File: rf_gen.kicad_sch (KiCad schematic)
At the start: 43 parts, among them J1 Conn_01x07_Male, J2 Conn_01x02_Female, J3 Conn_01x05_Male, J4 Jack-DC, Q1 GS61004B, Q2 G3R350MT12J, U1 NPC81074, U2 AP62150

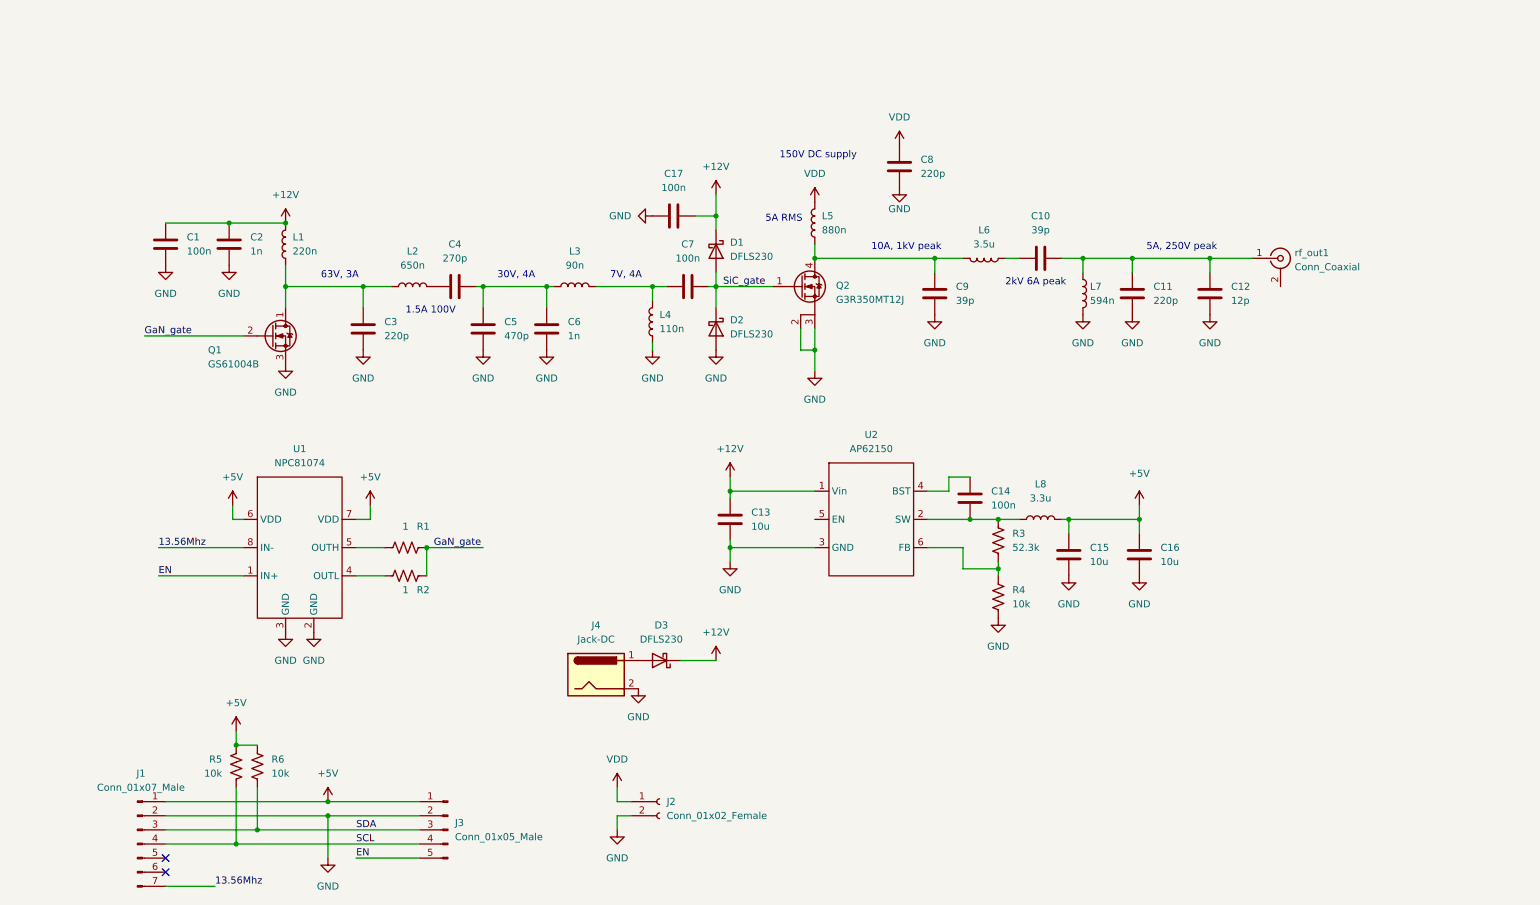
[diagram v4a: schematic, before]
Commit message: Added netclasses, test points, fixed buck regulator
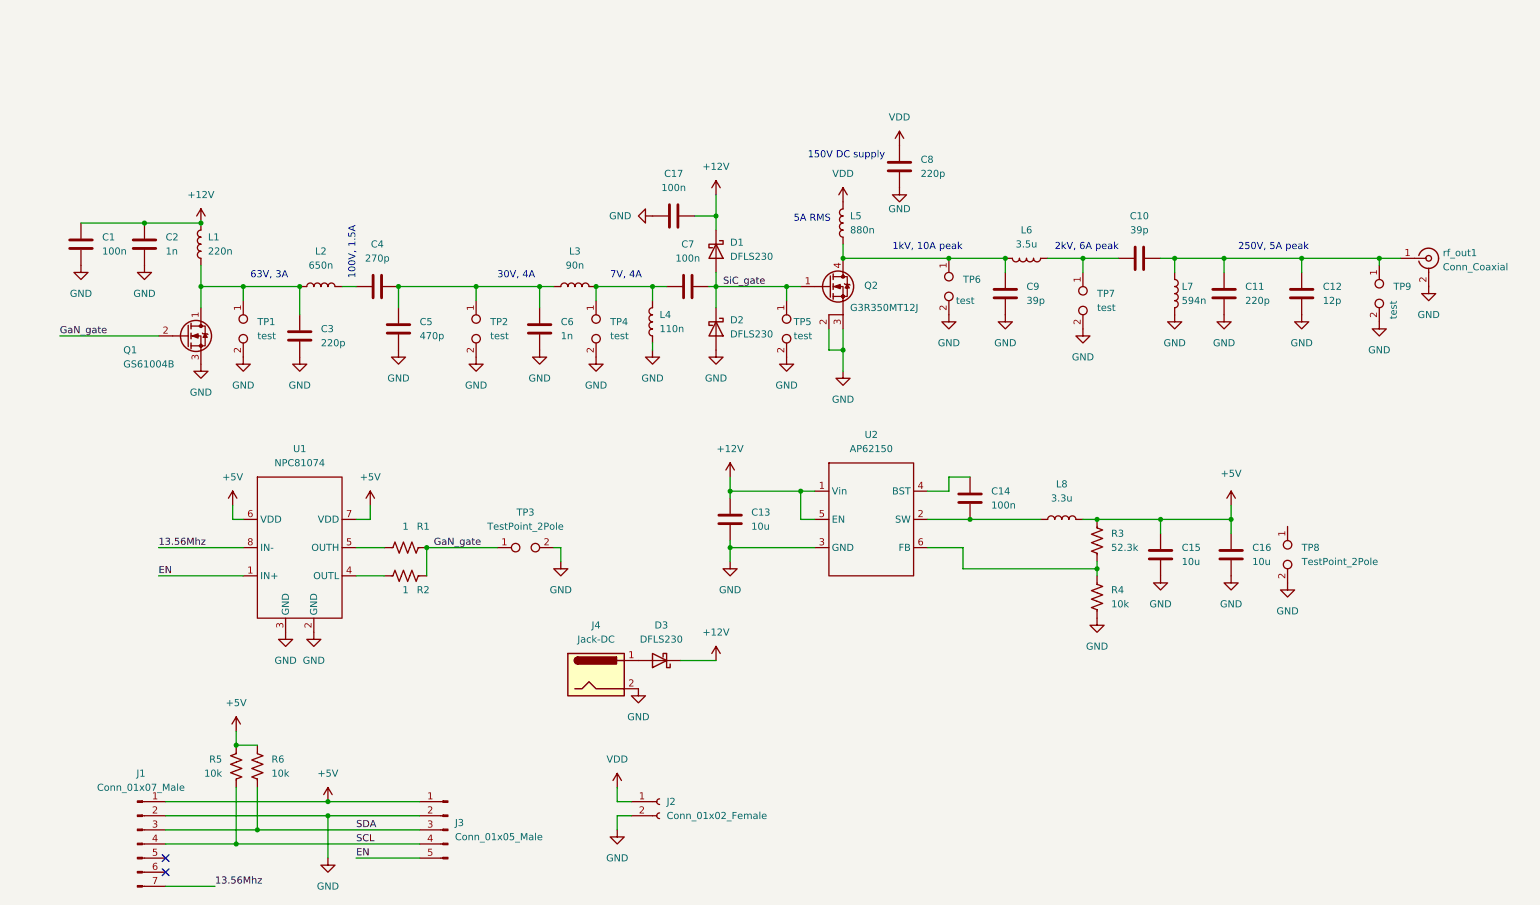
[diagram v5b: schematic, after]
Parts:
- added TP1, TP2, TP4, TP5, TP6, TP7, TP9: test, symbol Connector:TestPoint_2Pole
- added TP3, TP8: TestPoint_2Pole, symbol Connector:TestPoint_2Pole
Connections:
- net +12V: now also U2.5 (EN)
- net +5V: now also R3.1
- net GND: now also rf_out1.2 (Ext), TP1.2, TP2.2, TP3.2, TP4.2, TP5.2, TP6.2, TP7.2, TP8.2, TP9.2
- net GaN_gate: now also TP3.1
- net SiC_gate: now also TP5.1
- net at C4.2, C5.1, C6.1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: now also TP2.1
- net at C7.2, L3.2, L4.2: now also TP4.1
- net at C14.2, L8.1, U2.2 (SW): no longer R3.1
- net at C10.2, C11.1, C12.1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: now also TP9.1
- net at C3.2, L1.1, L2.1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: now also TP1.1
- net at C9.2, L5.1, L6.2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: now also TP6.1
- net at C10.1, L6.1: now also TP7.1
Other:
- note added: "100V, 1.5A"
- note added: "1kV, 10A peak"
- note added: "250V, 5A peak"
- note added: "2kV, 6A peak"
- note removed: "1.5A 100V"
- note removed: "10A, 1kV peak"
- note removed: "2kV 6A peak"
- note removed: "5A, 250V peak"
- moved on the sheet: C1, C10, C11, C12, C15, C16, C2, C3, C4, C5, C6, C9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

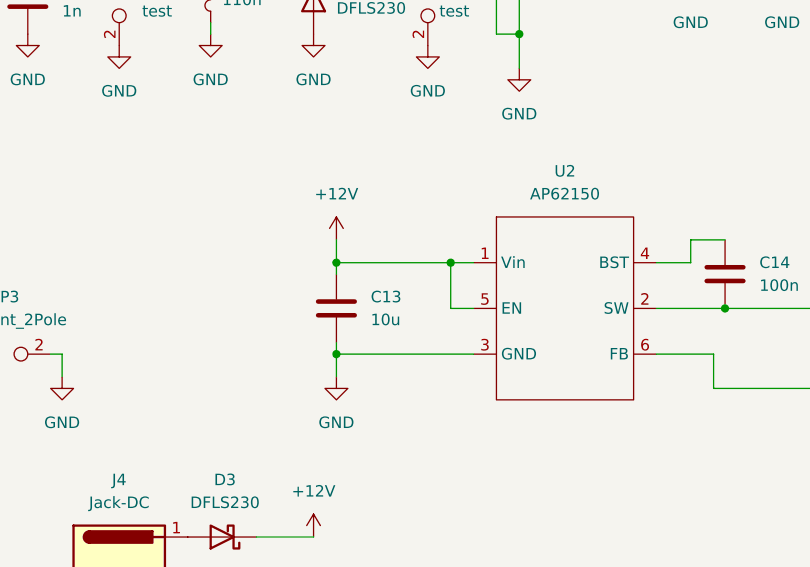
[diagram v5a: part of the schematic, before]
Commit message: Draft of trace routing
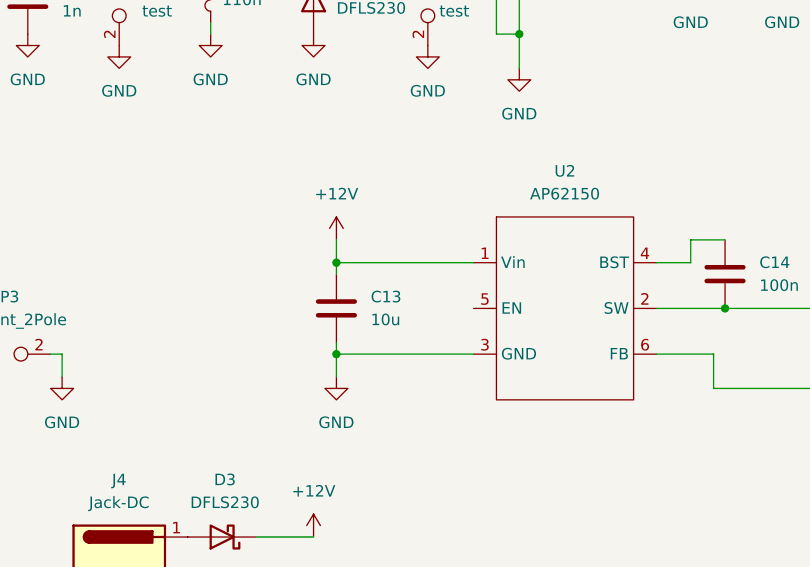
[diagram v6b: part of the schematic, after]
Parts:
- TP1, TP2, TP3, TP4, TP5, TP6, TP7, TP8, TP9: footprint (none) -> TestPoint:TestPoint_2Pads_Pitch5.08mm_Drill1.3mm
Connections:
- net +12V: no longer U2.5 (EN)
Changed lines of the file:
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@@
 (kicad_sch (version 20211123) (generator eeschema)
   (paper "A4")
-  (junction (at 157.48 116.84) (diameter 0) (color 0 0 0 0)
-  )
   (junction (at 110.49 80.01) (diameter 0) (color 0 0 0 0)
   )
@@
     (stroke (width 0) (type default) (color 0 0 0 0))
   )
-  (wire (pts (xy 157.48 121.92) (xy 157.48 116.84))
-    (stroke (width 0) (type default) (color 0 0 0 0))
-  )
   (wire (pts (xy 55.88 162.56) (xy 59.69 162.56))
     (stroke (width 0) (type default) (color 0 0 0 0))
@@
     (stroke (width 0) (type default) (color 0 0 0 0))
   )
-  (wire (pts (xy 144.78 116.84) (xy 157.48 116.84))
-    (stroke (width 0) (type default) (color 0 0 0 0))
-  )
   (wire (pts (xy 201.93 74.93) (xy 208.28 74.93))
     (stroke (width 0) (type default) (color 0 0 0 0))
@@
     (stroke (width 0) (type default) (color 0 0 0 0))
   )
-  (wire (pts (xy 160.02 121.92) (xy 157.48 121.92))
-    (stroke (width 0) (type default) (color 0 0 0 0))
-  )
   (wire (pts (xy 77.47 80.01) (xy 74.93 80.01))
     (stroke (width 0) (type default) (color 0 0 0 0))
@@
     (stroke (width 0) (type default) (color 0 0 0 0))
   )
-  (wire (pts (xy 157.48 116.84) (xy 160.02 116.84))
+  (wire (pts (xy 144.78 116.84) (xy 160.02 116.84))
     (stroke (width 0) (type default) (color 0 0 0 0))
   )
@@
       (effects (font (size 1.27 1.27)) (justify left))
     )
-    (property "Footprint" "" (id 2) (at 245.11 128.27 0)
+    (property "Footprint" "TestPoint:TestPoint_2Pads_Pitch5.08mm_Drill1.3mm" (id 2) (at 245.11 128.27 0)
       (effects (font (size 1.27 1.27)) hide)
     )
@@
       (effects (font (size 1.27 1.27)) (justify left))
     )
-    (property "Footprint" "" (id 2) (at 99.06 87.63 0)
+    (property "Footprint" "TestPoint:TestPoint_2Pads_Pitch5.08mm_Drill1.3mm" (id 2) (at 99.06 87.63 0)
       (effects (font (size 1.27 1.27)) hide)
     )
@@
       (effects (font (size 1.27 1.27)) (justify left))
     )
-    (property "Footprint" "" (id 2) (at 208.28 82.55 0)
+    (property "Footprint" "TestPoint:TestPoint_2Pads_Pitch5.08mm_Drill1.3mm" (id 2) (at 208.28 82.55 0)
       (effects (font (size 1.27 1.27)) hide)
     )
@@
       (effects (font (size 1.27 1.27)) (justify left))
     )
-    (property "Footprint" "" (id 2) (at 261.62 81.28 0)
+    (property "Footprint" "TestPoint:TestPoint_2Pads_Pitch5.08mm_Drill1.3mm" (id 2) (at 261.62 81.28 0)
       (effects (font (size 1.27 1.27)) hide)
     )
@@
     (property "Reference" "TP3" (id 0) (at 107.95 120.65 0))
     (property "Value" "TestPoint_2Pole" (id 1) (at 107.95 123.19 0))
-    (property "Footprint" "" (id 2) (at 107.95 127 0)
+    (property "Footprint" "TestPoint:TestPoint_2Pads_Pitch5.08mm_Drill1.3mm" (id 2) (at 107.95 127 0)
       (effects (font (size 1.27 1.27)) hide)
     )
@@
       (effects (font (size 1.27 1.27)) (justify left))
     )
-    (property "Footprint" "" (id 2) (at 120.65 87.63 0)
+    (property "Footprint" "TestPoint:TestPoint_2Pads_Pitch5.08mm_Drill1.3mm" (id 2) (at 120.65 87.63 0)
       (effects (font (size 1.27 1.27)) hide)
     )
@@
       (effects (font (size 1.27 1.27)) (justify left))
     )
-    (property "Footprint" "" (id 2) (at 57.15 87.63 0)
+    (property "Footprint" "TestPoint:TestPoint_2Pads_Pitch5.08mm_Drill1.3mm" (id 2) (at 57.15 87.63 0)
       (effects (font (size 1.27 1.27)) hide)
     )
@@
       (effects (font (size 1.27 1.27)) (justify left))
     )
-    (property "Footprint" "" (id 2) (at 184.15 80.01 0)
+    (property "Footprint" "TestPoint:TestPoint_2Pads_Pitch5.08mm_Drill1.3mm" (id 2) (at 184.15 80.01 0)
       (effects (font (size 1.27 1.27)) hide)
     )
@@
       (effects (font (size 1.27 1.27)) (justify left))
     )
-    (property "Footprint" "" (id 2) (at 154.94 87.63 0)
+    (property "Footprint" "TestPoint:TestPoint_2Pads_Pitch5.08mm_Drill1.3mm" (id 2) (at 154.94 87.63 0)
       (effects (font (size 1.27 1.27)) hide)
     )
@@
     )
     (path "/9e46c7f8-a513-4ff2-a7e6-e7adc86b0c60"
-      (reference "TP1") (unit 1) (value "test") (footprint "")
+      (reference "TP1") (unit 1) (value "test") (footprint "TestPoint:TestPoint_2Pads_Pitch5.08mm_Drill1.3mm")
     )
     (path "/380384f8-f2f9-4acb-82c0-d194cb47f844"
-      (reference "TP2") (unit 1) (value "test") (footprint "")
+      (reference "TP2") (unit 1) (value "test") (footprint "TestPoint:TestPoint_2Pads_Pitch5.08mm_Drill1.3mm")
     )
     (path "/75c06a4c-dfd4-4ed7-b3c2-af1e7ac28588"
-      (reference "TP3") (unit 1) (value "TestPoint_2Pole") (footprint "")
+      (reference "TP3") (unit 1) (value "TestPoint_2Pole") (footprint "TestPoint:TestPoint_2Pads_Pitch5.08mm_Drill1.3mm")
     )
     (path "/9a243108-930d-4114-9dcc-3f8fefa4acfd"
-      (reference "TP4") (unit 1) (value "test") (footprint "")
+      (reference "TP4") (unit 1) (value "test") (footprint "TestPoint:TestPoint_2Pads_Pitch5.08mm_Drill1.3mm")
     )
     (path "/e1db0c58-29d8-489b-9a95-02e5bb88fba5"
-      (reference "TP5") (unit 1) (value "test") (footprint "")
+      (reference "TP5") (unit 1) (value "test") (footprint "TestPoint:TestPoint_2Pads_Pitch5.08mm_Drill1.3mm")
     )
     (path "/cb32965e-963f-4082-9e02-ff21cd91984e"
-      (reference "TP6") (unit 1) (value "test") (footprint "")
+      (reference "TP6") (unit 1) (value "test") (footprint "TestPoint:TestPoint_2Pads_Pitch5.08mm_Drill1.3mm")
     )
     (path "/49587f3e-e4fc-4bf0-8d1d-a51cab304d0c"
-      (reference "TP7") (unit 1) (value "test") (footprint "")
+      (reference "TP7") (unit 1) (value "test") (footprint "TestPoint:TestPoint_2Pads_Pitch5.08mm_Drill1.3mm")
     )
     (path "/07035750-a09f-4f0d-b8da-574cc7129fe3"
-      (reference "TP8") (unit 1) (value "TestPoint_2Pole") (footprint "")
+      (reference "TP8") (unit 1) (value "TestPoint_2Pole") (footprint "TestPoint:TestPoint_2Pads_Pitch5.08mm_Drill1.3mm")
     )
     (path "/60d8926b-287a-43ee-89b3-bae467c7fd5e"
-      (reference "TP9") (unit 1) (value "test") (footprint "")
+      (reference "TP9") (unit 1) (value "test") (footprint "TestPoint:TestPoint_2Pads_Pitch5.08mm_Drill1.3mm")
     )
     (path "/05524bb0-81b6-47ef-ac3c-1b815742ae84"

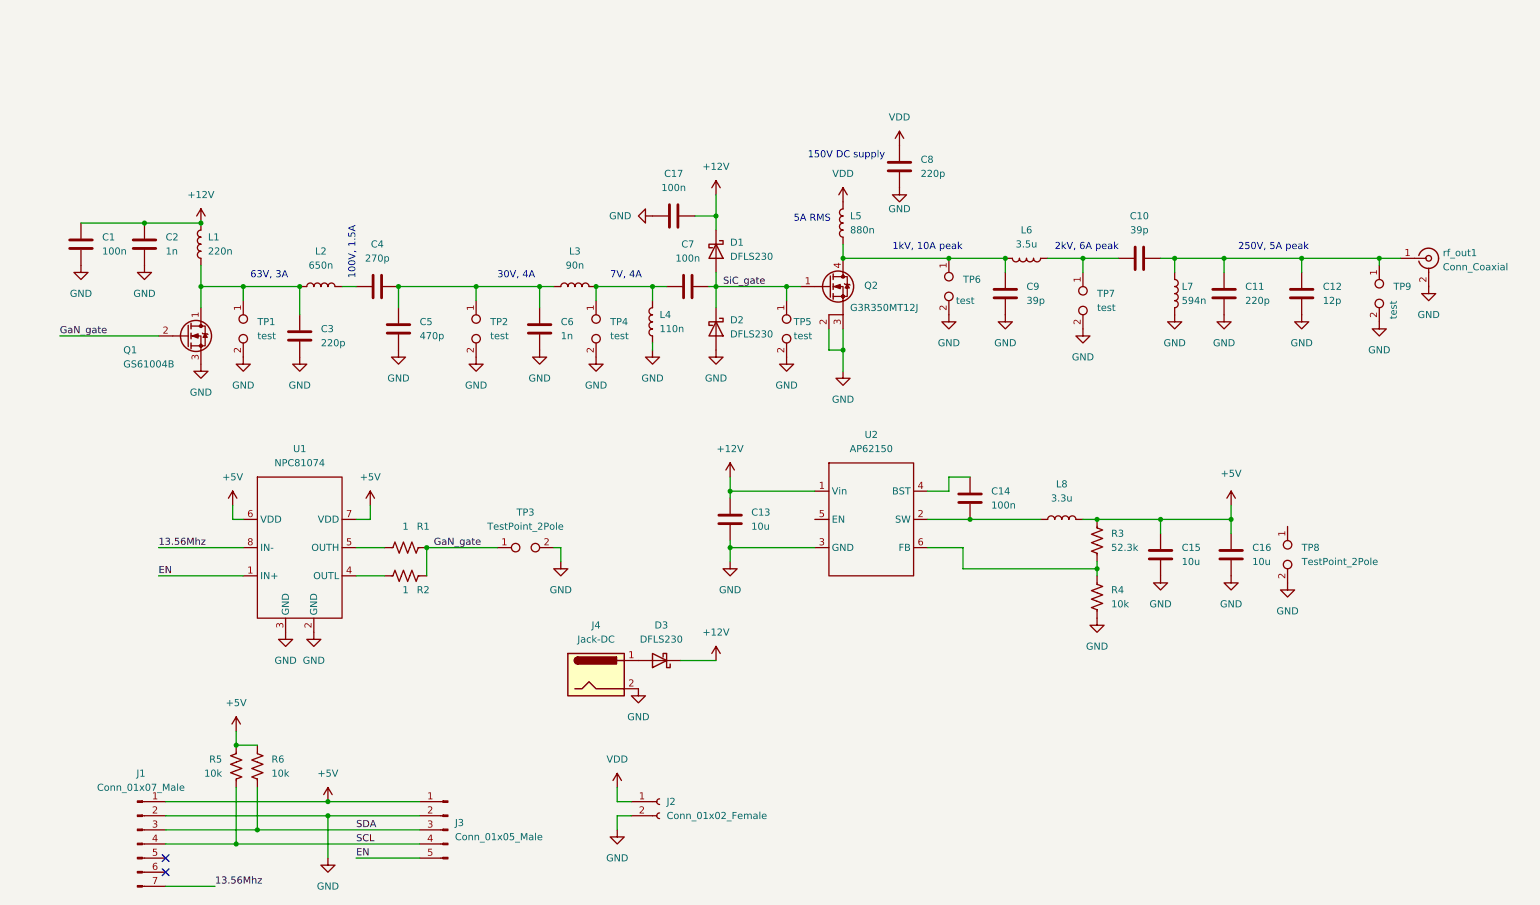
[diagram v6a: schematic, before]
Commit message: Finished routing
Replaced power inductor footprints with actual sizes
Placed test points that seemed useful, removed ones that didn't fit
Replaced RF connector and power input connectors
Added LED to indicate power
Added stitching vias
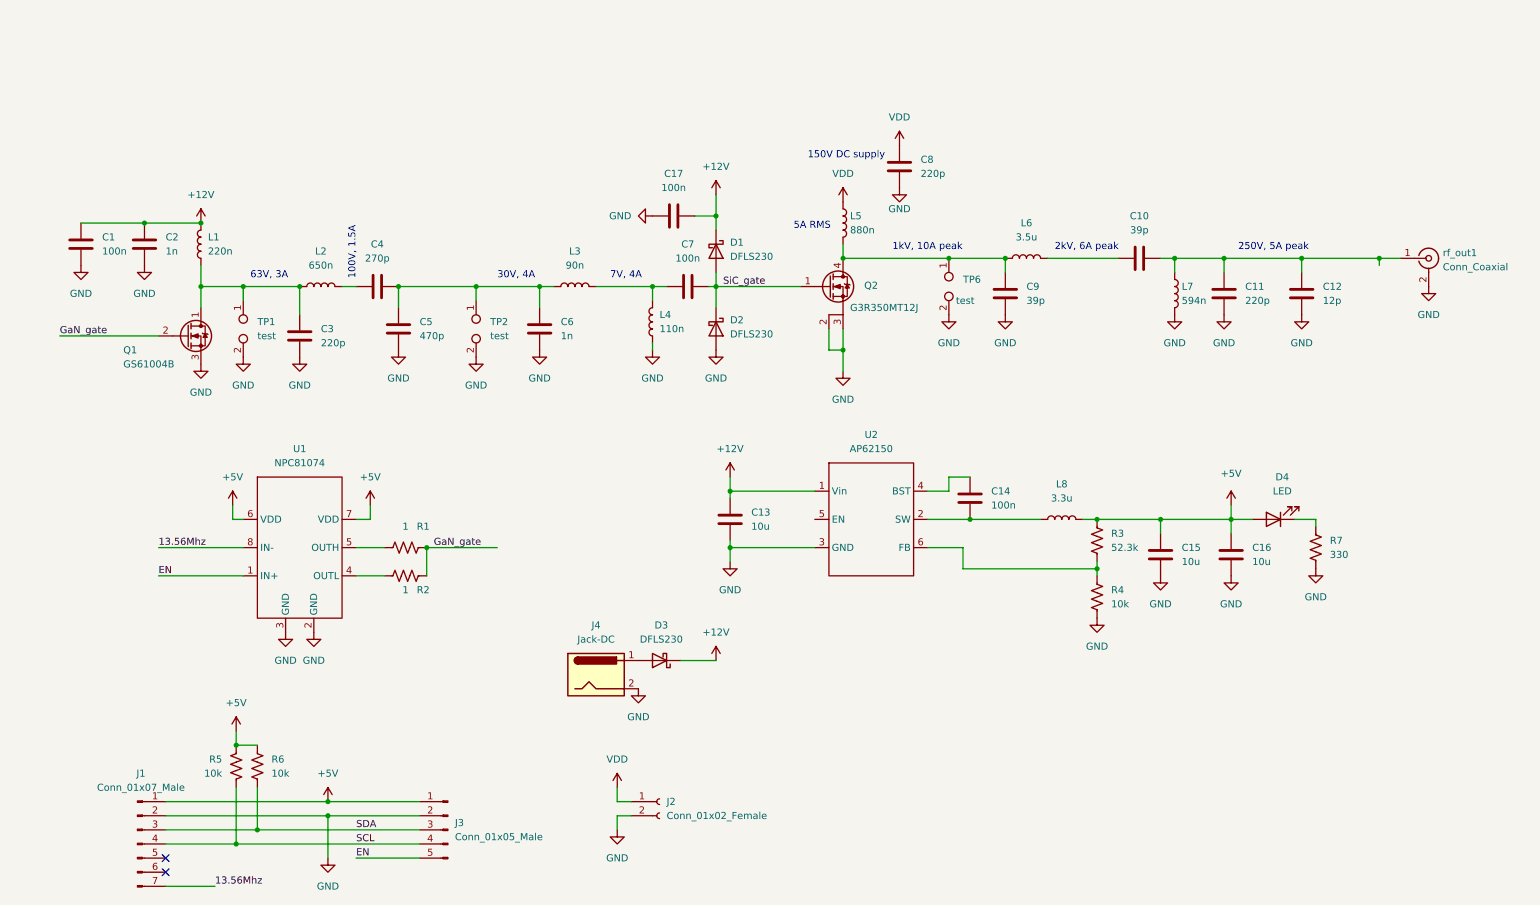
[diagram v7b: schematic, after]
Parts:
- removed TP3, TP8: TestPoint_2Pole, TestPoint:TestPoint_2Pads_Pitch5.08mm_Drill1.3mm, symbol Connector:TestPoint_2Pole
- removed TP4, TP5, TP7, TP9: test, TestPoint:TestPoint_2Pads_Pitch5.08mm_Drill1.3mm, symbol Connector:TestPoint_2Pole
- added D4: LED, LED_SMD:LED_0805_2012Metric, symbol Device:LED
- added R7: 330, Resistor_SMD:R_0805_2012Metric, symbol Device:R_US
- J2: footprint Connector_Phoenix_MC_HighVoltage:PhoenixContact_MCV_1,5_2-GF-5.08_1x02_P5.08mm_Vertical_ThreadedFlange -> Connector_Phoenix_MSTB:PhoenixContact_MSTBVA_2,5_2-G_1x02_P5.00mm_Vertical
- J4: footprint Connector_BarrelJack:BarrelJack_SwitchcraftConxall_RAPC10U_Horizontal -> Connector_Phoenix_MSTB:PhoenixContact_MSTBVA_2,5_2-G_1x02_P5.00mm_Vertical
- L5: footprint Inductor_THT:L_Axial_L17.5mm_D12.0mm_P20.32mm_Horizontal_Vishay_IM-10-46 -> rf_gen:inductor_air_15x15
- L6: footprint Inductor_THT:L_Toroid_Vertical_L28.6mm_W14.3mm_P11.43mm_Bourns_5700 -> rf_gen:inductor_core_25x18
- L7: footprint Inductor_THT:L_Toroid_Vertical_L10.0mm_W5.0mm_P5.08mm -> rf_gen:inductor_core_25x18
- Q2: footprint rf_gen:TO-263-7_nmos -> rf_gen:TO-263-7_heatsink
- rf_out1: footprint Connector_Coaxial:BNC_TEConnectivity_1478204_Vertical -> Connector_Coaxial:SMA_Molex_73251-1153_EdgeMount_Horizontal
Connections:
- net +5V: now also D4.2 (A)
- net GND: now also R7.2
- net VDD: now also L5.1; no longer L5.2
- net at C9.2, Q2.4 (D), TP6.1: now also L5.2, L6.1; no longer L5.1, L6.2
- net at C10.1: now also L6.2; no longer L6.1
- new net: D4.1 (K), R7.1
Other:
- moved on the sheet: L5, L6
